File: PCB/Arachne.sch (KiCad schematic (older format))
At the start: 0 parts

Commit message: PCB-Schema: Initialization of project
First sketch of power input and motor driver IC.
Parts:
- added C? (x2): 1uF (X7R), Capacitor_SMD:C_0805_2012Metric, symbol Device:C
- added C?: 100nF, Capacitor_SMD:C_0603_1608Metric, symbol Device:C
- added D? (x4): GREEN, LED_SMD:LED_0603_1608Metric_Castellated, symbol Motherboard-rescue:LED-Device
- added D? (x4): YELLOW, LED_SMD:LED_0603_1608Metric_Castellated, symbol Motherboard-rescue:LED-Device
- added J?: VMOT_A, Connector_Phoenix_MC:PhoenixContact_MC_1,5_4-G-3.5_1x04_P3.50mm_Horizontal, symbol Connector_Generic:Conn_01x04
- added Q?: 2N7002, Package_TO_SOT_SMD:SOT-23, symbol Device:Q_NMOS_GSD
- added Q?: AOD4189, Package_TO_SOT_SMD:TO-252-2, symbol Device:Q_PMOS_GDS
- added R?: 20k, Resistor_SMD:R_0603_1608Metric, symbol Device:R
- added R?: 180k, Resistor_SMD:R_0603_1608Metric, symbol Device:R
- added R? (x2): 10k, Resistor_SMD:R_0603_1608Metric, symbol Device:R
- added RN? (x2): 4x 120R, Resistor_SMD:R_Array_Convex_4x0603, symbol Motherboard-rescue:R_Pack04-Device
- added TP?: VMOT_A, TestPoint:TestPoint_THTPad_D1.5mm_Drill0.7mm, symbol Connector:TestPoint
- added TP?: IMOT_A, TestPoint:TestPoint_THTPad_D1.5mm_Drill0.7mm, symbol Connector:TestPoint
- added U?: ACS712xLCTR-20A, Package_SO:SOIC-8_3.9x4.9mm_P1.27mm, symbol Sensor_Current:ACS712xLCTR-20A
- added U?: STM32L432KCUx, Package_DFN_QFN:QFN-32-1EP_5x5mm_P0.5mm_EP3.45x3.45mm, symbol MCU_ST_STM32L4:STM32L432KCUx
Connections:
- net labels added: +12V, +3.3V, +5V, BUSY_A1, BUSY_A2, BUSY_A3, BUSY_A4, FLAG_A1, FLAG_A2, FLAG_A3, FLAG_A4, GND, I_MOT_A_MON, VMOT_A, V_MOT_A_MON
- wire segments 0 -> 82
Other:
- note added: "Power monitoring"
- note added: "Stepper signals"

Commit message: PCB-Schema: Update of labels in power input
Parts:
- removed C? (x2): 1uF (X7R), Capacitor_SMD:C_0805_2012Metric, symbol Device:C
- removed C?: 100nF, Capacitor_SMD:C_0603_1608Metric, symbol Device:C
- removed D? (x4): GREEN, LED_SMD:LED_0603_1608Metric_Castellated, symbol Motherboard-rescue:LED-Device
- removed D? (x4): YELLOW, LED_SMD:LED_0603_1608Metric_Castellated, symbol Motherboard-rescue:LED-Device
- removed J?: VMOT_A, Connector_Phoenix_MC:PhoenixContact_MC_1,5_4-G-3.5_1x04_P3.50mm_Horizontal, symbol Connector_Generic:Conn_01x04
- removed Q?: 2N7002, Package_TO_SOT_SMD:SOT-23, symbol Device:Q_NMOS_GSD
- removed Q?: AOD4189, Package_TO_SOT_SMD:TO-252-2, symbol Device:Q_PMOS_GDS
- removed R?: 20k, Resistor_SMD:R_0603_1608Metric, symbol Device:R
- removed R?: 180k, Resistor_SMD:R_0603_1608Metric, symbol Device:R
- removed R? (x2): 10k, Resistor_SMD:R_0603_1608Metric, symbol Device:R
- removed RN? (x2): 4x 120R, Resistor_SMD:R_Array_Convex_4x0603, symbol Motherboard-rescue:R_Pack04-Device
- removed TP?: VMOT_A, TestPoint:TestPoint_THTPad_D1.5mm_Drill0.7mm, symbol Connector:TestPoint
- removed TP?: IMOT_A, TestPoint:TestPoint_THTPad_D1.5mm_Drill0.7mm, symbol Connector:TestPoint
- removed U?: ACS712xLCTR-20A, Package_SO:SOIC-8_3.9x4.9mm_P1.27mm, symbol Sensor_Current:ACS712xLCTR-20A
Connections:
- net labels removed: +12V, +3.3V, +5V, BUSY_A1, BUSY_A2, BUSY_A3, BUSY_A4, FLAG_A1, FLAG_A2, FLAG_A3, FLAG_A4, GND, I_MOT_A_MON, VMOT_A, V_MOT_A_MON
- wire segments 82 -> 0
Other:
- note removed: "Power monitoring"
- note removed: "Stepper signals"
- moved on the sheet: U?

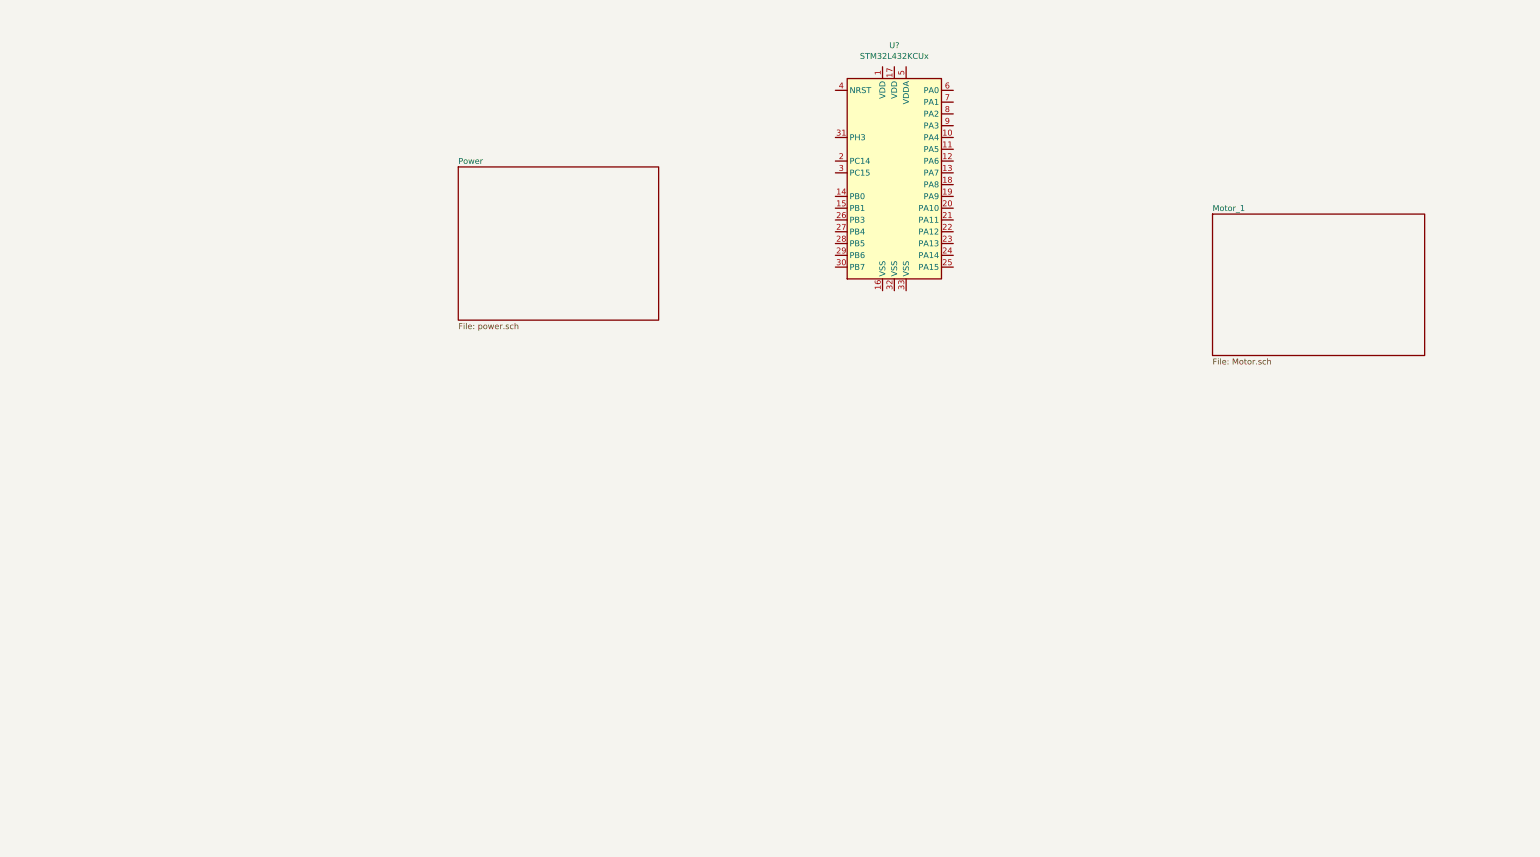
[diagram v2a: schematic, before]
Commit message: Schema: add other motors and create SPI connection
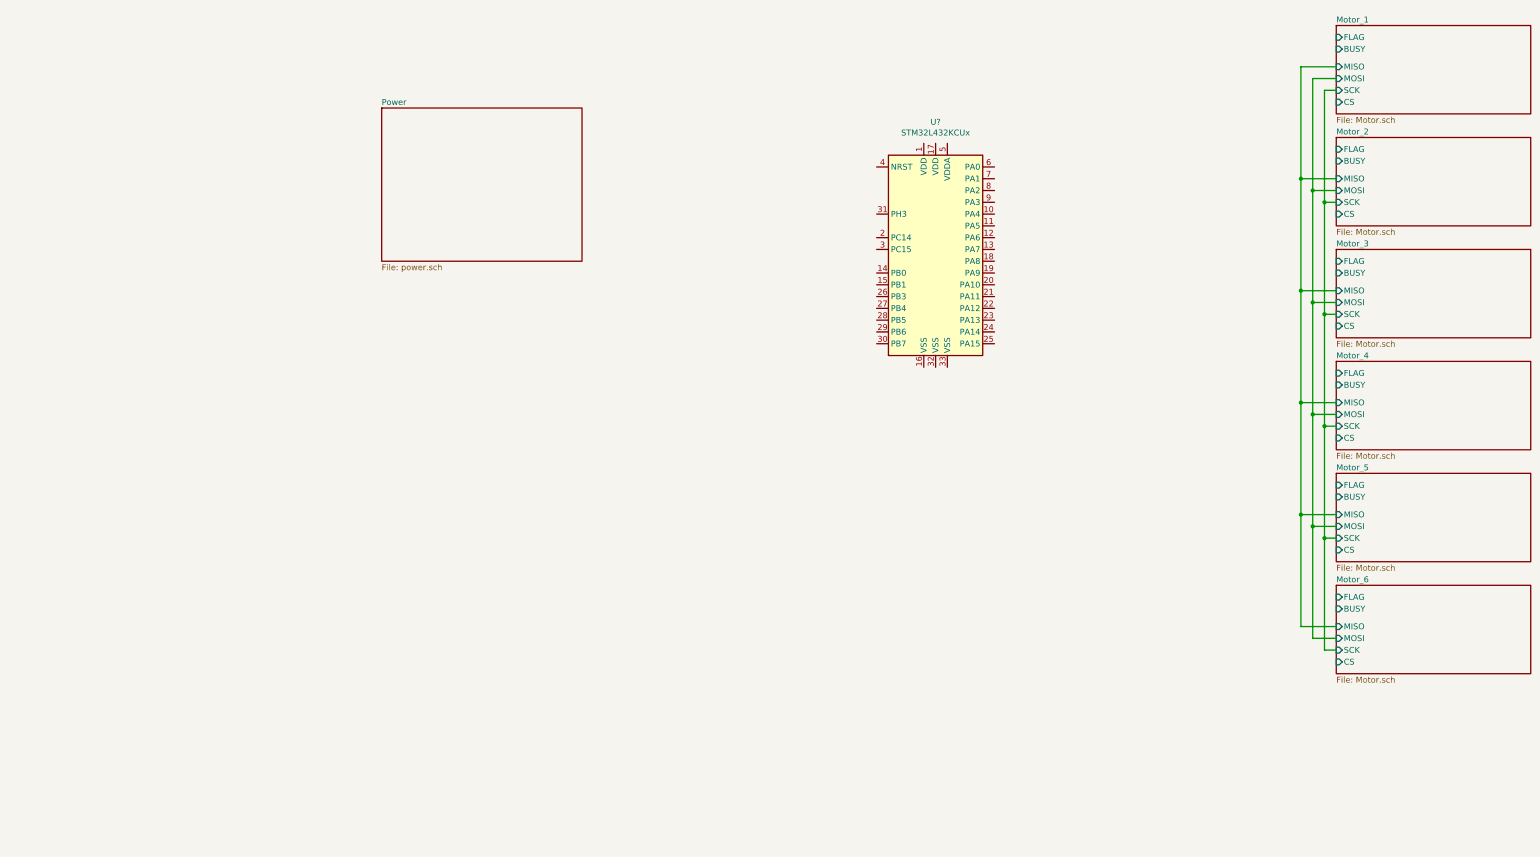
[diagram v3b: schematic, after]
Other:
- moved on the sheet: U?
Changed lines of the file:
@@
 EESchema Schematic File Version 4
 LIBS:Arachne-cache
-EELAYER 30 0
+EELAYER 29 0
 EELAYER END
 $Descr A4 11693 8268
@@
 L MCU_ST_STM32L4:STM32L432KCUx U?
 U 1 1 5D2F0D32
-P 5400 1950
-F 0 "U?" H 5400 3031 50  0000 C CNN
-F 1 "STM32L432KCUx" H 5400 2940 50  0000 C CNN
-F 2 "Package_DFN_QFN:QFN-32-1EP_5x5mm_P0.5mm_EP3.45x3.45mm" H 5000 1050 50  0001 R CNN
-F 3 "http://www.st.com/st-web-ui/static/active/en/resource/technical/document/datasheet/DM00257205.pdf" H 5400 1950 50  0001 C CNN
-	1    5400 1950
+P 5750 2600
+F 0 "U?" H 5750 3681 50  0000 C CNN
+F 1 "STM32L432KCUx" H 5750 3590 50  0000 C CNN
+F 2 "Package_DFN_QFN:QFN-32-1EP_5x5mm_P0.5mm_EP3.45x3.45mm" H 5350 1700 50  0001 R CNN
+F 3 "http://www.st.com/st-web-ui/static/active/en/resource/technical/document/datasheet/DM00257205.pdf" H 5750 2600 50  0001 C CNN
+	1    5750 2600
 	1    0    0    -1
 $EndComp
 $Sheet
-S 8100 2300 1800 1200
+S 9150 700  1650 750
 U 5D3521E4
 F0 "Motor_1" 50
 F1 "Motor.sch" 50
+F2 "FLAG" I L 9150 800 50
+F3 "BUSY" I L 9150 900 50
+F4 "CS" I L 9150 1350 50
+F5 "SCK" I L 9150 1250 50
+F6 "MOSI" I L 9150 1150 50
+F7 "MISO" I L 9150 1050 50
 $EndSheet
 $Sheet
-S 1700 1900 1700 1300
+S 1050 1400 1700 1300
 U 5D436602
 F0 "Power" 50
 F1 "power.sch" 50
 $EndSheet
+$Sheet
+S 9150 1650 1650 750
+U 5D4BFD94
+F0 "Motor_2" 50
+F1 "Motor.sch" 50
+F2 "FLAG" I L 9150 1750 50
+F3 "BUSY" I L 9150 1850 50
+F4 "CS" I L 9150 2300 50
+F5 "SCK" I L 9150 2200 50
+F6 "MOSI" I L 9150 2100 50
+F7 "MISO" I L 9150 2000 50
+$EndSheet
+$Sheet
+S 9150 2600 1650 750
+U 5D4C05D6
+F0 "Motor_3" 50
+F1 "Motor.sch" 50
+F2 "FLAG" I L 9150 2700 50
+F3 "BUSY" I L 9150 2800 50
+F4 "CS" I L 9150 3250 50
+F5 "SCK" I L 9150 3150 50
+F6 "MOSI" I L 9150 3050 50
+F7 "MISO" I L 9150 2950 50
+$EndSheet
+$Sheet
+S 9150 3550 1650 750
+U 5D4C05DE
+F0 "Motor_4" 50
+F1 "Motor.sch" 50
+F2 "FLAG" I L 9150 3650 50
+F3 "BUSY" I L 9150 3750 50
+F4 "CS" I L 9150 4200 50
+F5 "SCK" I L 9150 4100 50
+F6 "MOSI" I L 9150 4000 50
+F7 "MISO" I L 9150 3900 50
+$EndSheet
+$Sheet
+S 9150 4500 1650 750
+U 5D4C14A6
+F0 "Motor_5" 50
+F1 "Motor.sch" 50
+F2 "FLAG" I L 9150 4600 50
+F3 "BUSY" I L 9150 4700 50
+F4 "CS" I L 9150 5150 50
+F5 "SCK" I L 9150 5050 50
+F6 "MOSI" I L 9150 4950 50
+F7 "MISO" I L 9150 4850 50
+$EndSheet
+$Sheet
+S 9150 5450 1650 750
+U 5D4C14AE
+F0 "Motor_6" 50
+F1 "Motor.sch" 50
+F2 "FLAG" I L 9150 5550 50
+F3 "BUSY" I L 9150 5650 50
+F4 "CS" I L 9150 6100 50
+F5 "SCK" I L 9150 6000 50
+F6 "MOSI" I L 9150 5900 50
+F7 "MISO" I L 9150 5800 50
+$EndSheet
+Wire Wire Line
+	9150 1250 9050 1250
+Wire Wire Line
+	9050 1250 9050 2200
+Wire Wire Line
+	9050 2200 9150 2200
+Wire Wire Line
+	9050 2200 9050 3150
+Wire Wire Line
+	9050 3150 9150 3150
+Connection ~ 9050 2200
+Wire Wire Line
+	9050 3150 9050 4100
+Wire Wire Line
+	9050 4100 9150 4100
+Connection ~ 9050 3150
+Wire Wire Line
+	9050 4100 9050 5050
+Wire Wire Line
+	9050 5050 9150 5050
+Connection ~ 9050 4100
+Wire Wire Line
+	9050 5050 9050 6000
+Wire Wire Line
+	9050 6000 9150 6000
+Connection ~ 9050 5050
+Wire Wire Line
+	9150 5900 8950 5900
+Wire Wire Line
+	8950 5900 8950 4950
+Wire Wire Line
+	8950 4950 9150 4950
+Wire Wire Line
+	8950 4950 8950 4000
+Wire Wire Line
+	8950 4000 9150 4000
+Connection ~ 8950 4950
+Wire Wire Line
+	8950 4000 8950 3050
+Wire Wire Line
+	8950 3050 9150 3050
+Connection ~ 8950 4000
+Wire Wire Line
+	8950 3050 8950 2100
+Wire Wire Line
+	8950 2100 9150 2100
+Connection ~ 8950 3050
+Wire Wire Line
+	8950 2100 8950 1150
+Wire Wire Line
+	8950 1150 9150 1150
+Connection ~ 8950 2100
+Wire Wire Line
+	9150 5800 8850 5800
+Wire Wire Line
+	8850 5800 8850 4850
+Wire Wire Line
+	8850 4850 9150 4850
+Wire Wire Line
+	8850 4850 8850 3900
+Wire Wire Line
+	8850 3900 9150 3900
+Connection ~ 8850 4850
+Wire Wire Line
+	8850 3900 8850 2950
+Wire Wire Line
+	8850 2950 9150 2950
+Connection ~ 8850 3900
+Wire Wire Line
+	8850 2950 8850 2000
+Wire Wire Line
+	8850 2000 9150 2000
+Connection ~ 8850 2950
+Wire Wire Line
+	8850 2000 8850 1050
+Wire Wire Line
+	8850 1050 9150 1050
+Connection ~ 8850 2000
 $EndSCHEMATC

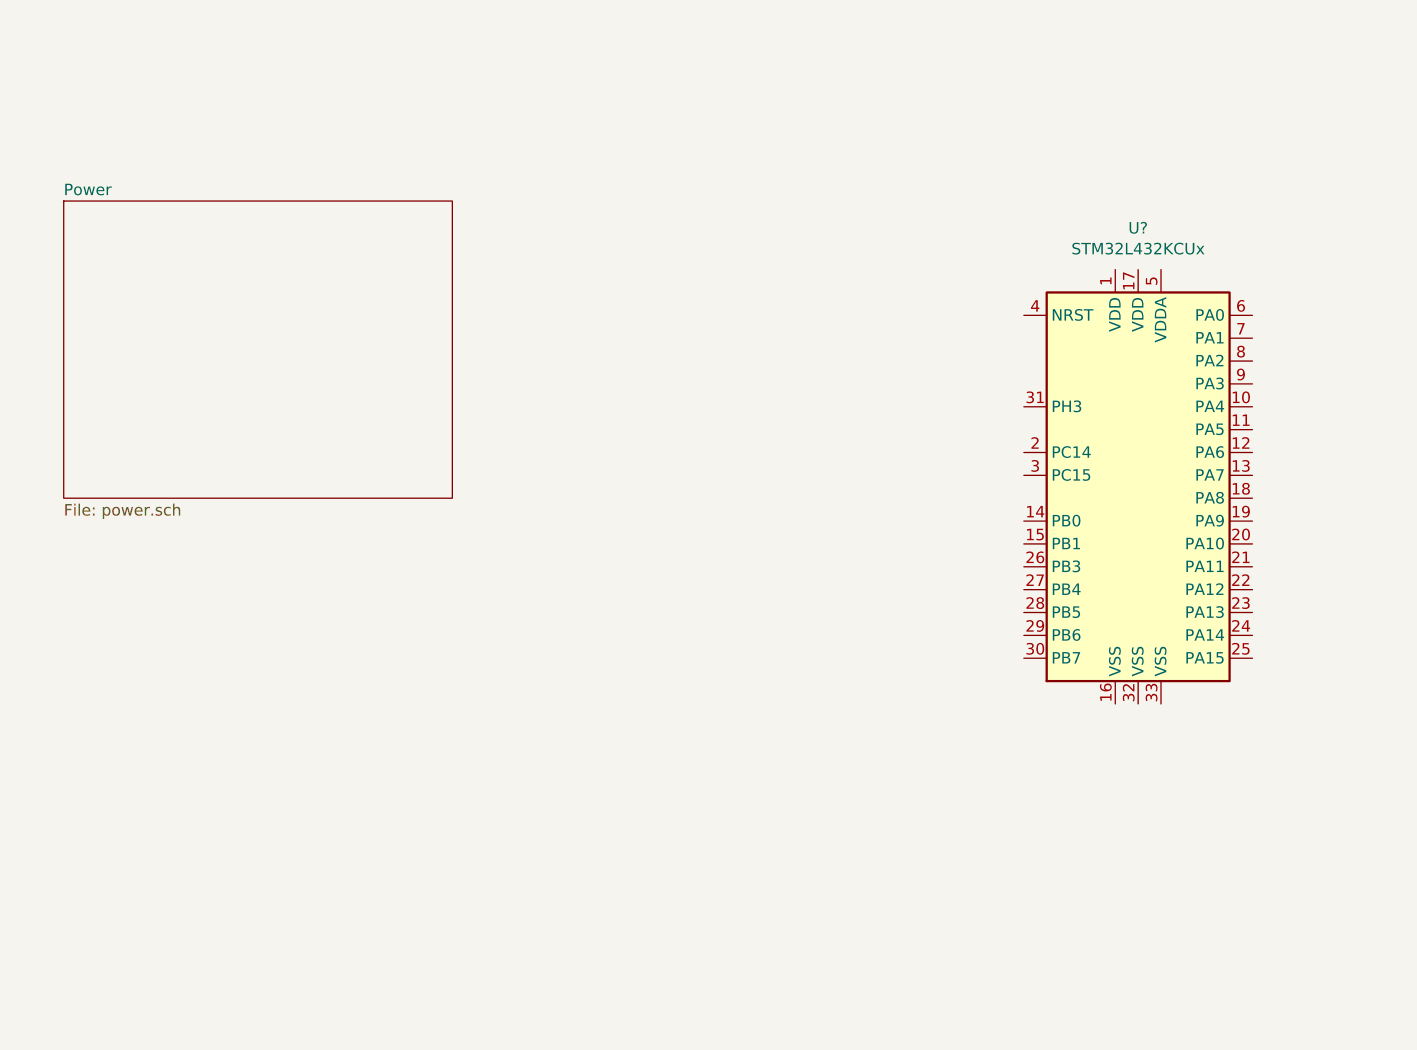
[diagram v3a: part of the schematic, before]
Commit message: Schema: add Interface schema, remove old mcu, add divider to current measuring
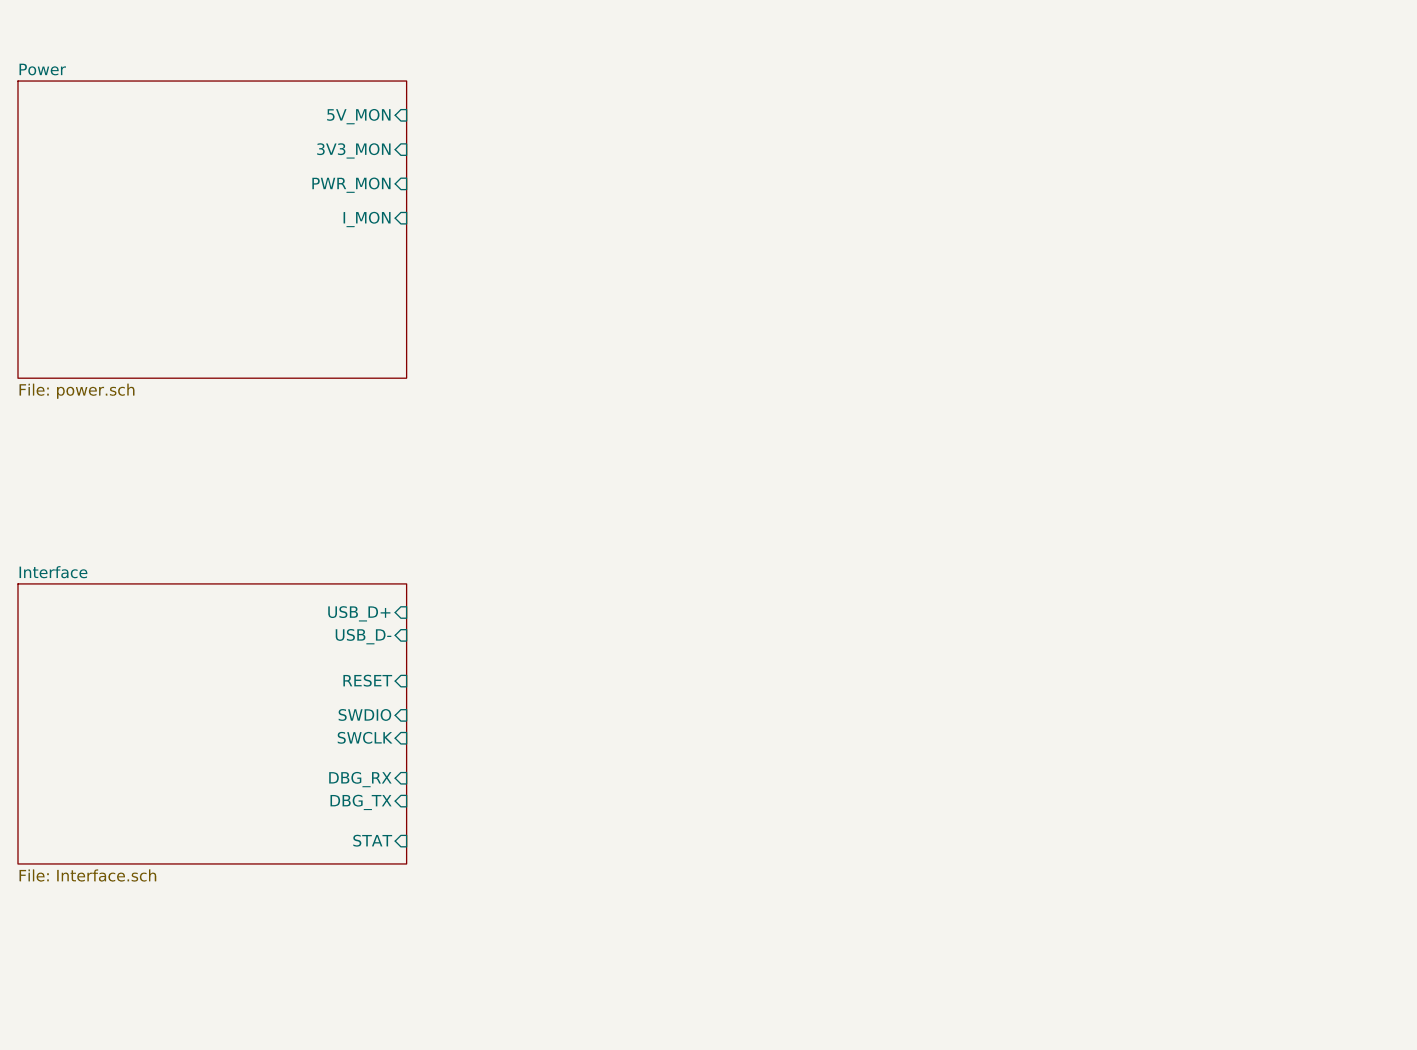
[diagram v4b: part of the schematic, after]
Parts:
- removed U?: STM32L432KCUx, Package_DFN_QFN:QFN-32-1EP_5x5mm_P0.5mm_EP3.45x3.45mm, symbol MCU_ST_STM32L4:STM32L432KCUx
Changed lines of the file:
@@
 EESchema Schematic File Version 4
-LIBS:Arachne-cache
-EELAYER 29 0
+EELAYER 30 0
 EELAYER END
 $Descr A4 11693 8268
 encoding utf-8
-Sheet 1 3
+Sheet 1 9
 Title "Arachne"
 Date "2019-07-16"
@@
 Comment4 ""
 $EndDescr
-$Comp
-L MCU_ST_STM32L4:STM32L432KCUx U?
-U 1 1 5D2F0D32
-P 5750 2600
-F 0 "U?" H 5750 3681 50  0000 C CNN
-F 1 "STM32L432KCUx" H 5750 3590 50  0000 C CNN
-F 2 "Package_DFN_QFN:QFN-32-1EP_5x5mm_P0.5mm_EP3.45x3.45mm" H 5350 1700 50  0001 R CNN
-F 3 "http://www.st.com/st-web-ui/static/active/en/resource/technical/document/datasheet/DM00257205.pdf" H 5750 2600 50  0001 C CNN
-	1    5750 2600
-	1    0    0    -1
-$EndComp
 $Sheet
 S 9150 700  1650 750
@@
 F6 "MOSI" I L 9150 1150 50
 F7 "MISO" I L 9150 1050 50
-$EndSheet
-$Sheet
-S 1050 1400 1700 1300
-U 5D436602
-F0 "Power" 50
-F1 "power.sch" 50
 $EndSheet
 $Sheet
@@
 	8850 1050 9150 1050
 Connection ~ 8850 2000
+$Sheet
+S 850  875  1700 1300
+U 5D436602
+F0 "Power" 50
+F1 "power.sch" 50
+F2 "5V_MON" I R 2550 1025 50
+F3 "3V3_MON" I R 2550 1175 50
+F4 "PWR_MON" I R 2550 1325 50
+F5 "I_MON" I R 2550 1475 50
+$EndSheet
+$Sheet
+S 850  3075 1700 1225
+U 5E43C48F
+F0 "Interface" 50
+F1 "Interface.sch" 50
+F2 "USB_D+" I R 2550 3200 50
+F3 "USB_D-" I R 2550 3300 50
+F4 "RESET" I R 2550 3500 50
+F5 "SWDIO" I R 2550 3650 50
+F6 "SWCLK" I R 2550 3750 50
+F7 "DBG_RX" I R 2550 3925 50
+F8 "DBG_TX" I R 2550 4025 50
+F9 "STAT" I R 2550 4200 50
+$EndSheet
 $EndSCHEMATC
